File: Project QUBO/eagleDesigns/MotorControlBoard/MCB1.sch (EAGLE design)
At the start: 14 parts, among them U1 PCA9685

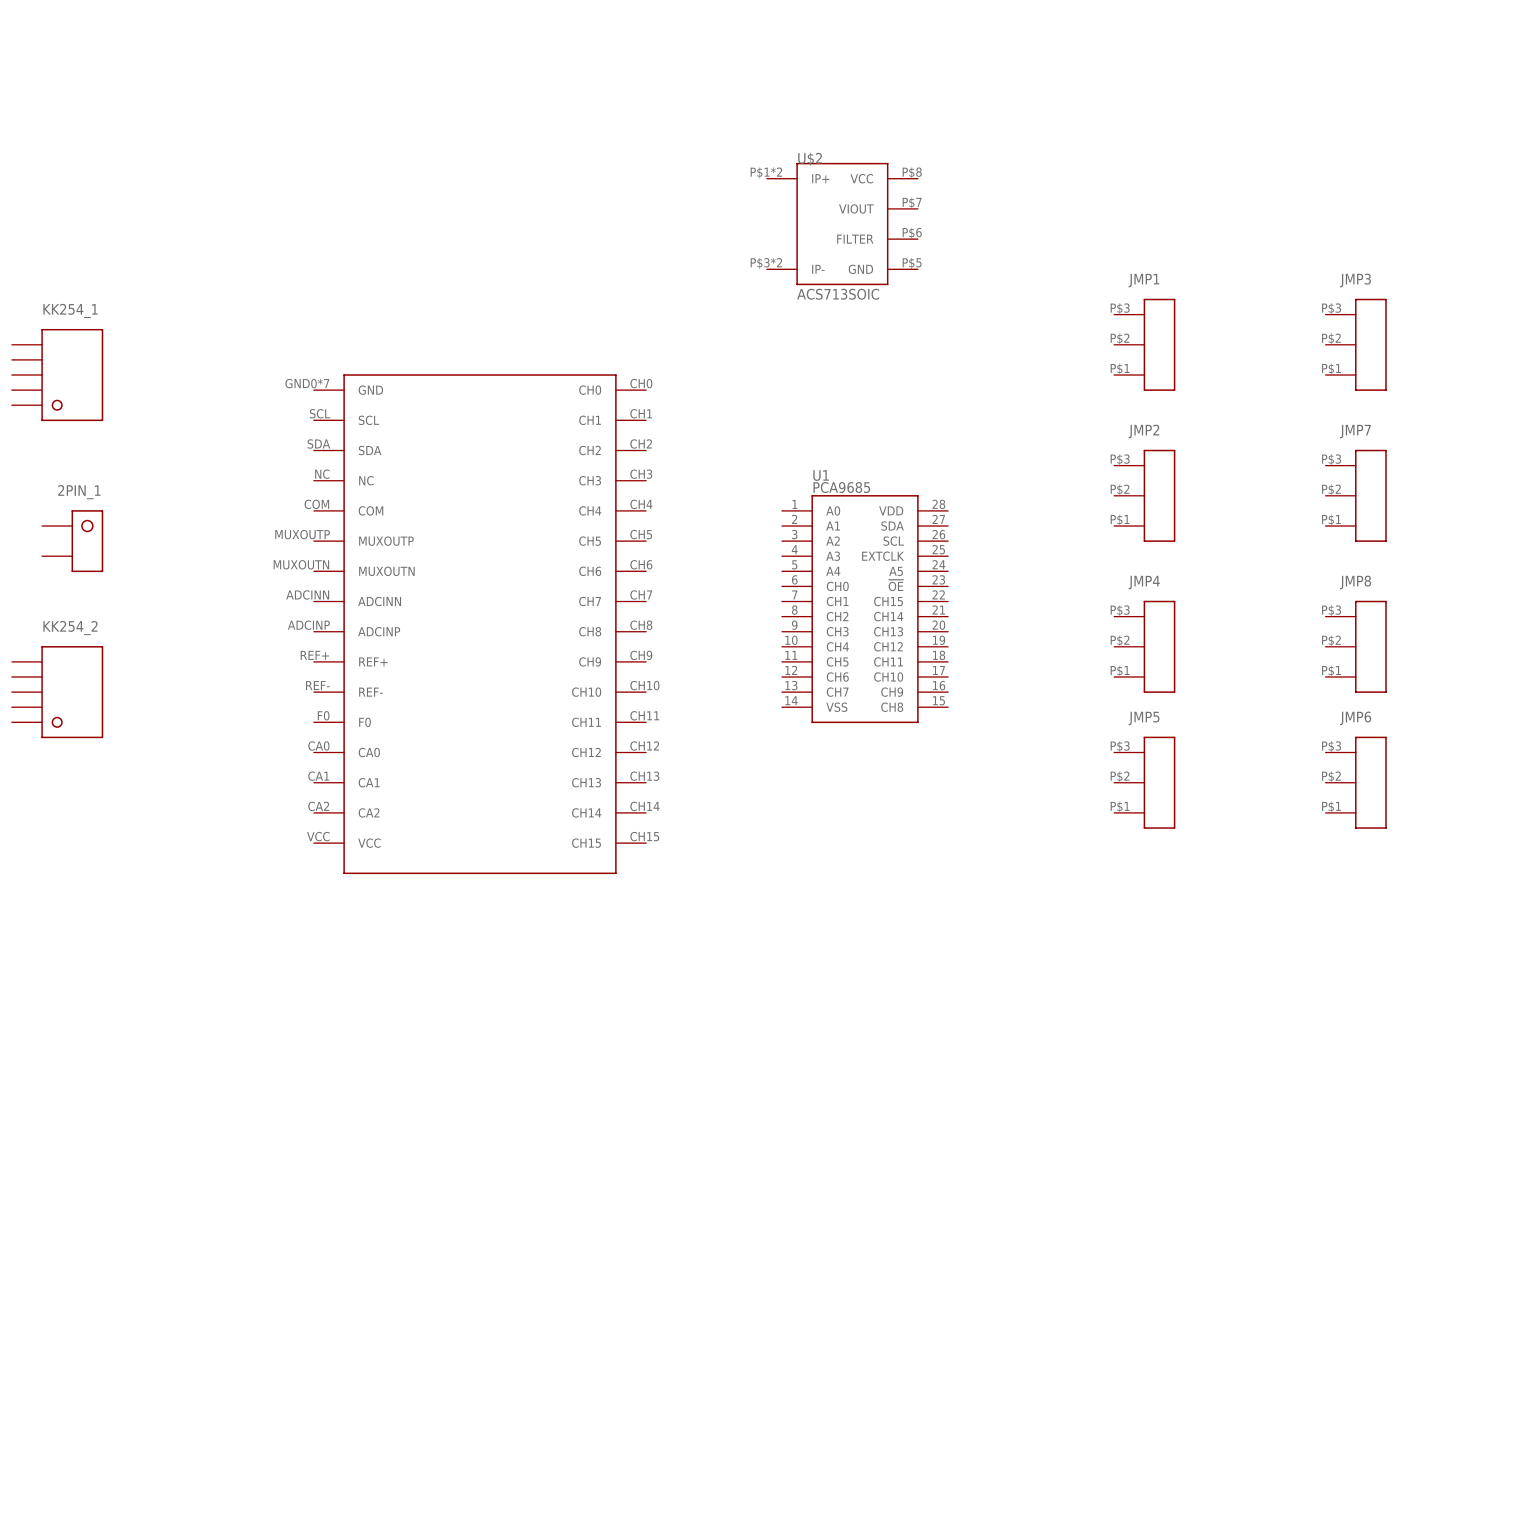
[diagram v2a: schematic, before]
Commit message: 
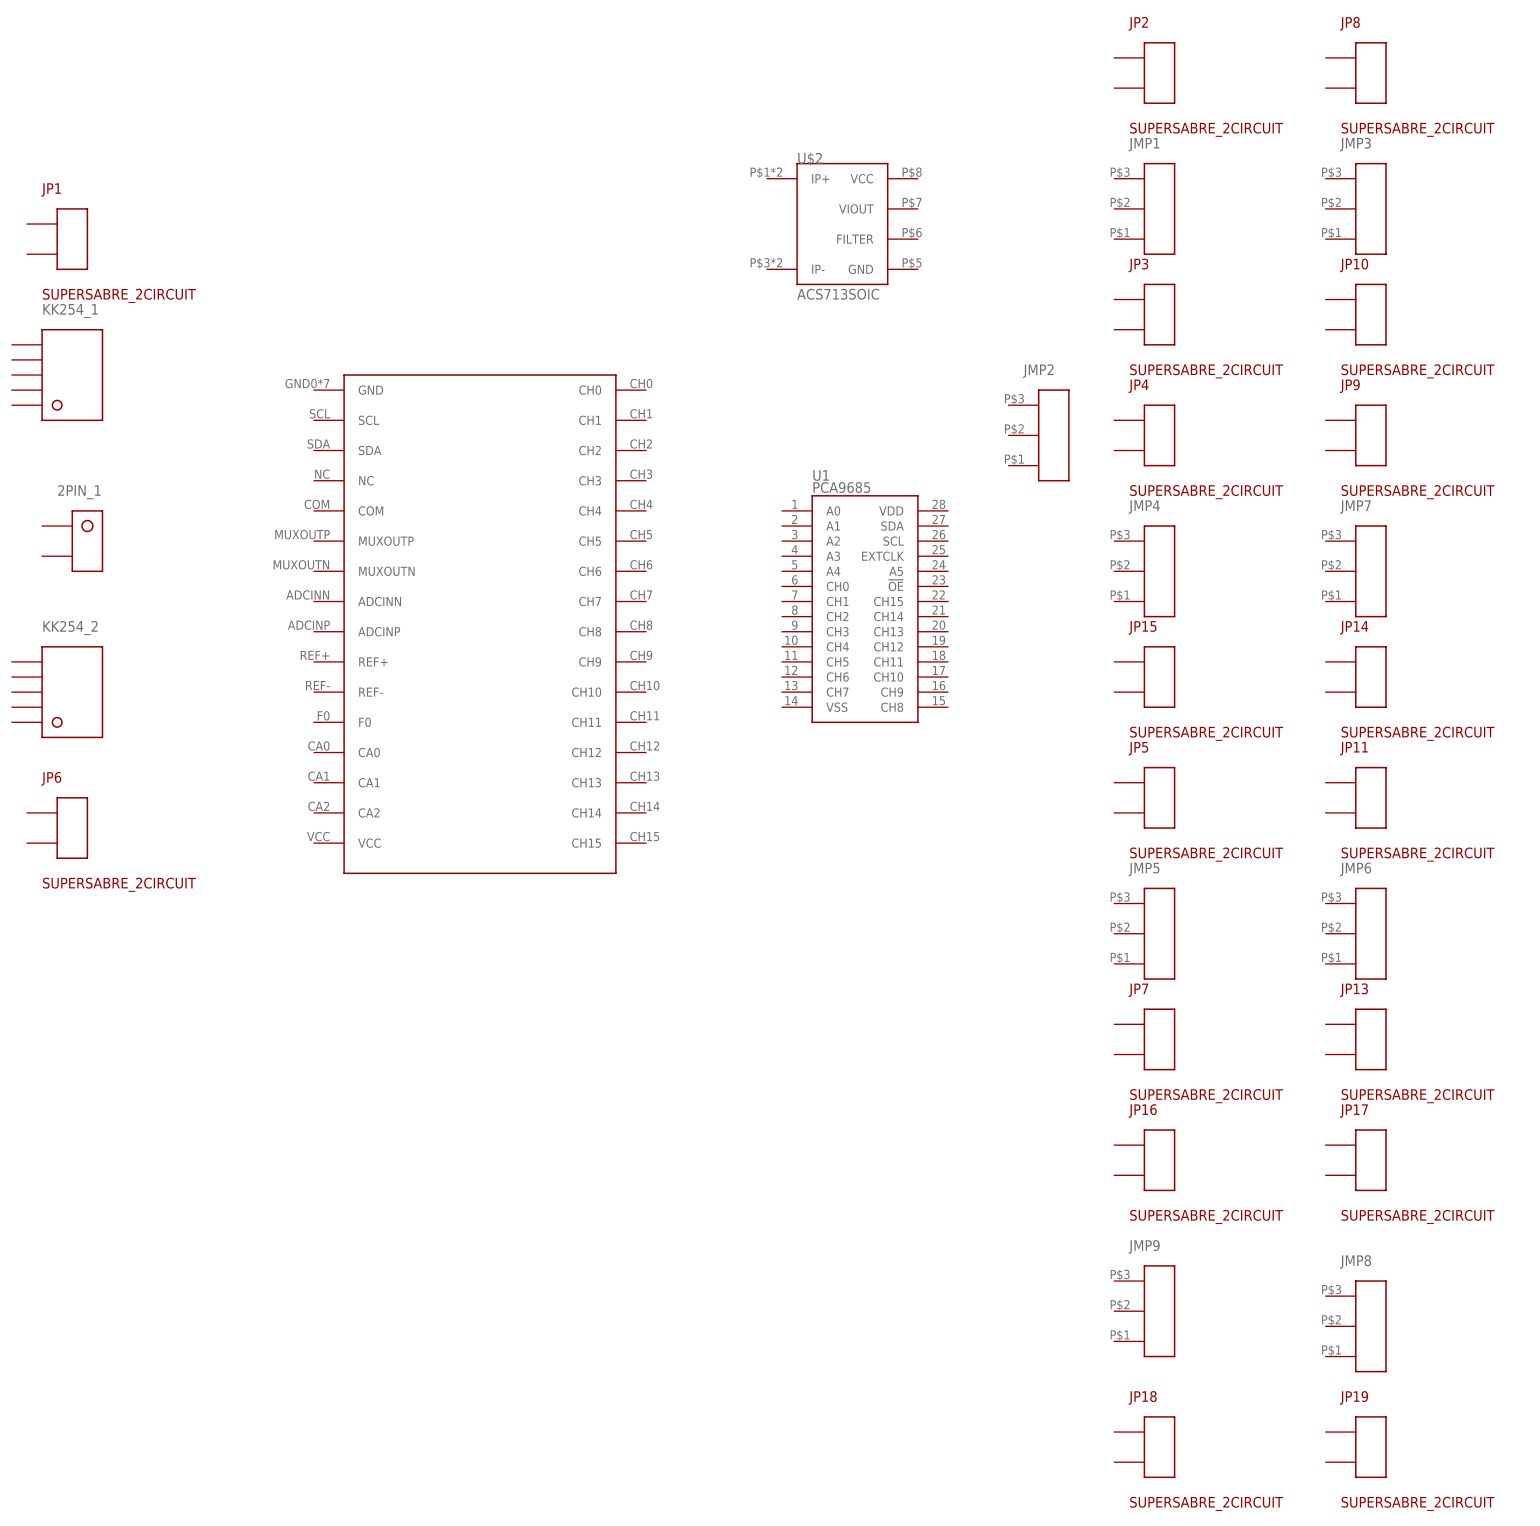
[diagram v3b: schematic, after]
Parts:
- added JMP9: (no value), molex:KK254_VERT_3PIN22-10-2031
- added JP1, JP10, JP11, JP13, JP14, JP15, JP16, JP17, JP18, JP19, JP2, JP3, JP4, JP5, JP6, JP7, JP8, JP9: SUPERSABRE_2CIRCUIT, molex:SUPERSABRE_2CIRCUIT
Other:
- moved on the sheet: JMP1, JMP2, JMP3, JMP4, JMP5, JMP6, JMP7, JMP8
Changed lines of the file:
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@@
 <grid distance="0.1" unitdist="inch" unit="inch" style="lines" multiple="1" display="no" altdistance="0.01" altunitdist="inch" altunit="inch"/>
 <layers>
-<layer number="1" name="Top" color="4" fill="1" visible="no" active="no"/>
-<layer number="16" name="Bottom" color="1" fill="1" visible="no" active="no"/>
-<layer number="17" name="Pads" color="2" fill="1" visible="no" active="no"/>
-<layer number="18" name="Vias" color="2" fill="1" visible="no" active="no"/>
-<layer number="19" name="Unrouted" color="6" fill="1" visible="no" active="no"/>
-<layer number="20" name="Dimension" color="15" fill="1" visible="no" active="no"/>
-<layer number="21" name="tPlace" color="15" fill="1" visible="no" active="no"/>
-<layer number="22" name="bPlace" color="7" fill="1" visible="no" active="no"/>
-<layer number="23" name="tOrigins" color="15" fill="1" visible="no" active="no"/>
-<layer number="24" name="bOrigins" color="15" fill="1" visible="no" active="no"/>
-<layer number="25" name="tNames" color="7" fill="1" visible="no" active="no"/>
-<layer number="26" name="bNames" color="7" fill="1" visible="no" active="no"/>
-<layer number="27" name="tValues" color="7" fill="1" visible="no" active="no"/>
-<layer number="28" name="bValues" color="7" fill="1" visible="no" active="no"/>
+<layer number="1" name="Top" color="4" fill="1" visible="yes" active="no"/>
+<layer number="16" name="Bottom" color="1" fill="1" visible="yes" active="no"/>
+<layer number="17" name="Pads" color="2" fill="1" visible="yes" active="no"/>
+<layer number="18" name="Vias" color="2" fill="1" visible="yes" active="no"/>
+<layer number="19" name="Unrouted" color="6" fill="1" visible="yes" active="no"/>
+<layer number="20" name="Dimension" color="15" fill="1" visible="yes" active="no"/>
+<layer number="21" name="tPlace" color="15" fill="1" visible="yes" active="no"/>
+<layer number="22" name="bPlace" color="7" fill="1" visible="yes" active="no"/>
+<layer number="23" name="tOrigins" color="15" fill="1" visible="yes" active="no"/>
+<layer number="24" name="bOrigins" color="15" fill="1" visible="yes" active="no"/>
+<layer number="25" name="tNames" color="7" fill="1" visible="yes" active="no"/>
+<layer number="26" name="bNames" color="7" fill="1" visible="yes" active="no"/>
+<layer number="27" name="tValues" color="7" fill="1" visible="yes" active="no"/>
+<layer number="28" name="bValues" color="7" fill="1" visible="yes" active="no"/>
 <layer number="29" name="tStop" color="7" fill="3" visible="no" active="no"/>
 <layer number="30" name="bStop" color="7" fill="6" visible="no" active="no"/>
@@
 <layer number="35" name="tGlue" color="7" fill="4" visible="no" active="no"/>
 <layer number="36" name="bGlue" color="7" fill="5" visible="no" active="no"/>
-<layer number="37" name="tTest" color="7" fill="1" visible="no" active="no"/>
-<layer number="38" name="bTest" color="7" fill="1" visible="no" active="no"/>
+<layer number="37" name="tTest" color="7" fill="1" visible="yes" active="no"/>
+<layer number="38" name="bTest" color="7" fill="1" visible="yes" active="no"/>
 <layer number="39" name="tKeepout" color="4" fill="11" visible="no" active="no"/>
 <layer number="40" name="bKeepout" color="1" fill="11" visible="no" active="no"/>
@@
 <layer number="44" name="Drills" color="7" fill="1" visible="no" active="no"/>
 <layer number="45" name="Holes" color="7" fill="1" visible="no" active="no"/>
-<layer number="46" name="Milling" color="3" fill="1" visible="no" active="no"/>
-<layer number="47" name="Measures" color="7" fill="1" visible="no" active="no"/>
-<layer number="48" name="Document" color="7" fill="1" visible="no" active="no"/>
-<layer number="49" name="Reference" color="7" fill="1" visible="no" active="no"/>
-<layer number="50" name="dxf" color="7" fill="1" visible="no" active="no"/>
-<layer number="51" name="tDocu" color="14" fill="1" visible="no" active="no"/>
-<layer number="52" name="bDocu" color="7" fill="1" visible="no" active="no"/>
-<layer number="53" name="tGND_GNDA" color="7" fill="9" visible="no" active="no"/>
-<layer number="54" name="bGND_GNDA" color="1" fill="9" visible="no" active="no"/>
-<layer number="56" name="wert" color="7" fill="1" visible="no" active="no"/>
-<layer number="57" name="tCAD" color="7" fill="1" visible="no" active="no"/>
-<layer number="59" name="tCarbon" color="7" fill="1" visible="no" active="no"/>
-<layer number="60" name="bCarbon" color="7" fill="1" visible="no" active="no"/>
+<layer number="46" name="Milling" color="3" fill="1" visible="yes" active="no"/>
+<layer number="47" name="Measures" color="7" fill="1" visible="yes" active="no"/>
+<layer number="48" name="Document" color="7" fill="1" visible="yes" active="no"/>
+<layer number="49" name="Reference" color="7" fill="1" visible="yes" active="no"/>
+<layer number="50" name="dxf" color="7" fill="1" visible="yes" active="no"/>
+<layer number="51" name="tDocu" color="14" fill="1" visible="yes" active="no"/>
+<layer number="52" name="bDocu" color="7" fill="1" visible="yes" active="no"/>
+<layer number="53" name="tGND_GNDA" color="7" fill="9" visible="yes" active="no"/>
+<layer number="54" name="bGND_GNDA" color="1" fill="9" visible="yes" active="no"/>
+<layer number="56" name="wert" color="7" fill="1" visible="yes" active="no"/>
+<layer number="57" name="tCAD" color="7" fill="1" visible="yes" active="no"/>
+<layer number="59" name="tCarbon" color="7" fill="1" visible="yes" active="no"/>
+<layer number="60" name="bCarbon" color="7" fill="1" visible="yes" active="no"/>
 <layer number="90" name="Modules" color="5" fill="1" visible="yes" active="yes"/>
 <layer number="91" name="Nets" color="2" fill="1" visible="yes" active="yes"/>
@@
 <part name="JMP7" library="molex" deviceset="KK254_VERT_3PIN" device="22-10-2031"/>
 <part name="JMP8" library="molex" deviceset="KK254_VERT_3PIN" device="22-10-2031"/>
+<part name="JP1" library="molex" deviceset="SUPERSABRE_2CIRCUIT" device=""/>
+<part name="JP2" library="molex" deviceset="SUPERSABRE_2CIRCUIT" device=""/>
+<part name="JP3" library="molex" deviceset="SUPERSABRE_2CIRCUIT" device=""/>
+<part name="JP4" library="molex" deviceset="SUPERSABRE_2CIRCUIT" device=""/>
+<part name="JP5" library="molex" deviceset="SUPERSABRE_2CIRCUIT" device=""/>
+<part name="JP7" library="molex" deviceset="SUPERSABRE_2CIRCUIT" device=""/>
+<part name="JP8" library="molex" deviceset="SUPERSABRE_2CIRCUIT" device=""/>
+<part name="JP9" library="molex" deviceset="SUPERSABRE_2CIRCUIT" device=""/>
+<part name="JP10" library="molex" deviceset="SUPERSABRE_2CIRCUIT" device=""/>
+<part name="JP11" library="molex" deviceset="SUPERSABRE_2CIRCUIT" device=""/>
+<part name="JP13" library="molex" deviceset="SUPERSABRE_2CIRCUIT" device=""/>
+<part name="JP14" library="molex" deviceset="SUPERSABRE_2CIRCUIT" device=""/>
+<part name="JP15" library="molex" deviceset="SUPERSABRE_2CIRCUIT" device=""/>
+<part name="JP16" library="molex" deviceset="SUPERSABRE_2CIRCUIT" device=""/>
+<part name="JP17" library="molex" deviceset="SUPERSABRE_2CIRCUIT" device=""/>
+<part name="JMP9" library="molex" deviceset="KK254_VERT_3PIN" device="22-10-2031"/>
+<part name="JP18" library="molex" deviceset="SUPERSABRE_2CIRCUIT" device=""/>
+<part name="JP19" library="molex" deviceset="SUPERSABRE_2CIRCUIT" device=""/>
+<part name="JP6" library="molex" deviceset="SUPERSABRE_2CIRCUIT" device=""/>
 </parts>
 <sheets>
@@
 <instance part="KK254_1" gate="G$1" x="-116.84" y="101.6"/>
 <instance part="KK254_2" gate="G$1" x="-116.84" y="48.26"/>
-<instance part="JMP3" gate="JMP1" x="101.6" y="106.68"/>
-<instance part="JMP1" gate="JMP1" x="66.04" y="106.68"/>
-<instance part="JMP2" gate="JMP1" x="66.04" y="81.28"/>
-<instance part="JMP4" gate="JMP1" x="66.04" y="55.88"/>
-<instance part="JMP5" gate="JMP1" x="66.04" y="33.02"/>
-<instance part="JMP6" gate="JMP1" x="101.6" y="33.02"/>
-<instance part="JMP7" gate="JMP1" x="101.6" y="81.28"/>
-<instance part="JMP8" gate="JMP1" x="101.6" y="55.88"/>
+<instance part="JMP3" gate="JMP1" x="101.6" y="129.54"/>
+<instance part="JMP1" gate="JMP1" x="66.04" y="129.54"/>
+<instance part="JMP2" gate="JMP1" x="48.26" y="91.44"/>
+<instance part="JMP4" gate="JMP1" x="66.04" y="68.58"/>
+<instance part="JMP5" gate="JMP1" x="66.04" y="7.62"/>
+<instance part="JMP6" gate="JMP1" x="101.6" y="7.62"/>
+<instance part="JMP7" gate="JMP1" x="101.6" y="68.58"/>
+<instance part="JMP8" gate="JMP1" x="101.6" y="-58.42"/>
+<instance part="JP1" gate="G$1" x="-124.46" y="124.46"/>
+<instance part="JP2" gate="G$1" x="58.42" y="152.4"/>
+<instance part="JP3" gate="G$1" x="58.42" y="111.76"/>
+<instance part="JP4" gate="G$1" x="58.42" y="91.44"/>
+<instance part="JP5" gate="G$1" x="58.42" y="30.48"/>
+<instance part="JP7" gate="G$1" x="58.42" y="-10.16"/>
+<instance part="JP8" gate="G$1" x="93.98" y="152.4"/>
+<instance part="JP9" gate="G$1" x="93.98" y="91.44"/>
+<instance part="JP10" gate="G$1" x="93.98" y="111.76"/>
+<instance part="JP11" gate="G$1" x="93.98" y="30.48"/>
+<instance part="JP13" gate="G$1" x="93.98" y="-10.16"/>
+<instance part="JP14" gate="G$1" x="93.98" y="50.8"/>
+<instance part="JP15" gate="G$1" x="58.42" y="50.8"/>
+<instance part="JP16" gate="G$1" x="58.42" y="-30.48"/>
+<instance part="JP17" gate="G$1" x="93.98" y="-30.48"/>
+<instance part="JMP9" gate="JMP1" x="66.04" y="-55.88"/>
+<instance part="JP18" gate="G$1" x="58.42" y="-78.74"/>
+<instance part="JP19" gate="G$1" x="93.98" y="-78.74"/>
+<instance part="JP6" gate="G$1" x="-124.46" y="25.4"/>
 </instances>
 <busses>

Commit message: edited motor board
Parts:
- removed JMP1, JMP2, JMP3, JMP4, JMP5, JMP6, JMP7, JMP8, JMP9: (no value), molex:KK254_VERT_3PIN22-10-2031
- removed JP1, JP10, JP11, JP13, JP14, JP15, JP16, JP17, JP18, JP19, JP2, JP3, JP4, JP5, JP6, JP7, JP8, JP9: SUPERSABRE_2CIRCUIT, molex:SUPERSABRE_2CIRCUIT
- removed KK254_1, KK254_2: (no value), molex:KK254_VERT_5PIN
- added 2PIN_10, 2PIN_2, 2PIN_3, 2PIN_4, 2PIN_5, 2PIN_6, 2PIN_7, 2PIN_8, 2PIN_9: (no value), molex:KK254_VERT_2PIN22-29-2021
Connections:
- new net 5V: 2PIN_10.P$1, U$1.VCC, U$2.VCC, U1.VDD
- new net 5VGND: 2PIN_10.P$2, 2PIN_2.P$2, 2PIN_3.P$2, 2PIN_4.P$2, 2PIN_5.P$2, 2PIN_6.P$2, 2PIN_7.P$2, 2PIN_8.P$2, 2PIN_9.P$2, U$1.GND, U$2.GND, U1.VSS
- new net PWM0: 2PIN_2.P$1, U1.CH0
- new net PWM1: 2PIN_3.P$1, U1.CH1
- new net PWM2: 2PIN_4.P$1, U1.CH2
- new net PWM3: 2PIN_5.P$1, U1.CH3
- new net PWM4: 2PIN_6.P$1, U1.CH4
- new net PWM5: 2PIN_7.P$1, U1.CH5
- new net PWM6: 2PIN_8.P$1, U1.CH6
- new net PWM7: 2PIN_9.P$1, U1.CH7
- new net SCL: 2PIN_1.P$2, U$1.SCL, U1.SCL
- new net SDA: 2PIN_1.P$1, U$1.SDA, U1.SDA
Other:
- moved on the sheet: U$2, U1
